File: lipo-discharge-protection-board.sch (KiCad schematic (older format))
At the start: 49 parts, among them J1 XT60, J2 Barrel_Jack, J3 2_PIN_SCREW, J4 Screw_Terminal_01x04, J5 Conn_02x02_Top_Bottom, Q1 AO3400A, Q2 AO3401A, Q3 AO3401A, Q4 AO3401A, Q5 AO3401A, U1 XL6009_module, U2 OPAMP

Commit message: Added alarm circuit
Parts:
- added D?: LED, symbol Device:LED
- added R?: 330R, Capacitor_SMD:C_0805_2012Metric_Pad1.18x1.45mm_HandSolder, symbol Device:R
- added R?: 220R, symbol Device:R
- added U?: L7805, symbol Regulator_Linear:L7805
- added U?: EL3H7, Package_DIP:DIP-4_W7.62mm, symbol Isolator:SFH617A-1
- Q2, Q3, Q4, Q5: LCSC C15127 -> AO3401A
- R1, R10, R11, R12, R13, R14, R15, R16, R2, R3, R4, R6, R7, R8, R9: footprint Resistor_SMD:R_0805_2012Metric_Pad1.20x1.40mm_HandSolder -> Capacitor_SMD:C_0805_2012Metric_Pad1.18x1.45mm_HandSolder
- R5: value 0R -> 0; footprint Resistor_SMD:R_0805_2012Metric_Pad1.20x1.40mm_HandSolder -> Capacitor_SMD:C_0805_2012Metric_Pad1.18x1.45mm_HandSolder
- U1: symbol lipo-discharge-protection-board-rescue:XL6009_module-xl6009_module -> xl6009_module:XL6009_module
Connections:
- net GND: now also R?.1, U?.2, U?.2 (GND)
- net at U?.3: now also U?.1 (IN)
- new net: D?.2 (A), R?.2, U?.3 (OUT)
- new net: R?.1, U?.1
- new net: D?.1 (K), R?.2
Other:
- moved on the sheet: J4, J5

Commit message: Added components for the alarm circuit and fixed wrong footprints
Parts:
- D2: renamed from D?; footprint (none) -> LED_SMD:LED_0805_2012Metric_Pad1.15x1.40mm_HandSolder
- R1, R10, R11, R12, R13, R14, R15, R16, R2, R3, R4, R5, R6, R7, R8, R9: footprint Capacitor_SMD:C_0805_2012Metric_Pad1.18x1.45mm_HandSolder -> Resistor_SMD:R_0805_2012Metric_Pad1.20x1.40mm_HandSolder
- R17, R18, R20: renamed from R?; footprint Capacitor_SMD:C_0805_2012Metric_Pad1.18x1.45mm_HandSolder -> Resistor_SMD:R_0805_2012Metric_Pad1.20x1.40mm_HandSolder
- R19: renamed from R?; footprint (none) -> Resistor_SMD:R_0805_2012Metric_Pad1.20x1.40mm_HandSolder
- U1: symbol xl6009_module:XL6009_module -> lipo-discharge-protection-board-rescue:XL6009_module-xl6009_module
- U4: renamed from U?; footprint (none) -> Package_TO_SOT_SMD:SOT-89-3_Handsoldering
- U5: renamed from U?; footprint Package_DIP:DIP-4_W7.62mm -> lipo-discharge-protection-board:SOIC127P700X210-4N
- gave numbers to parts that had none: 3

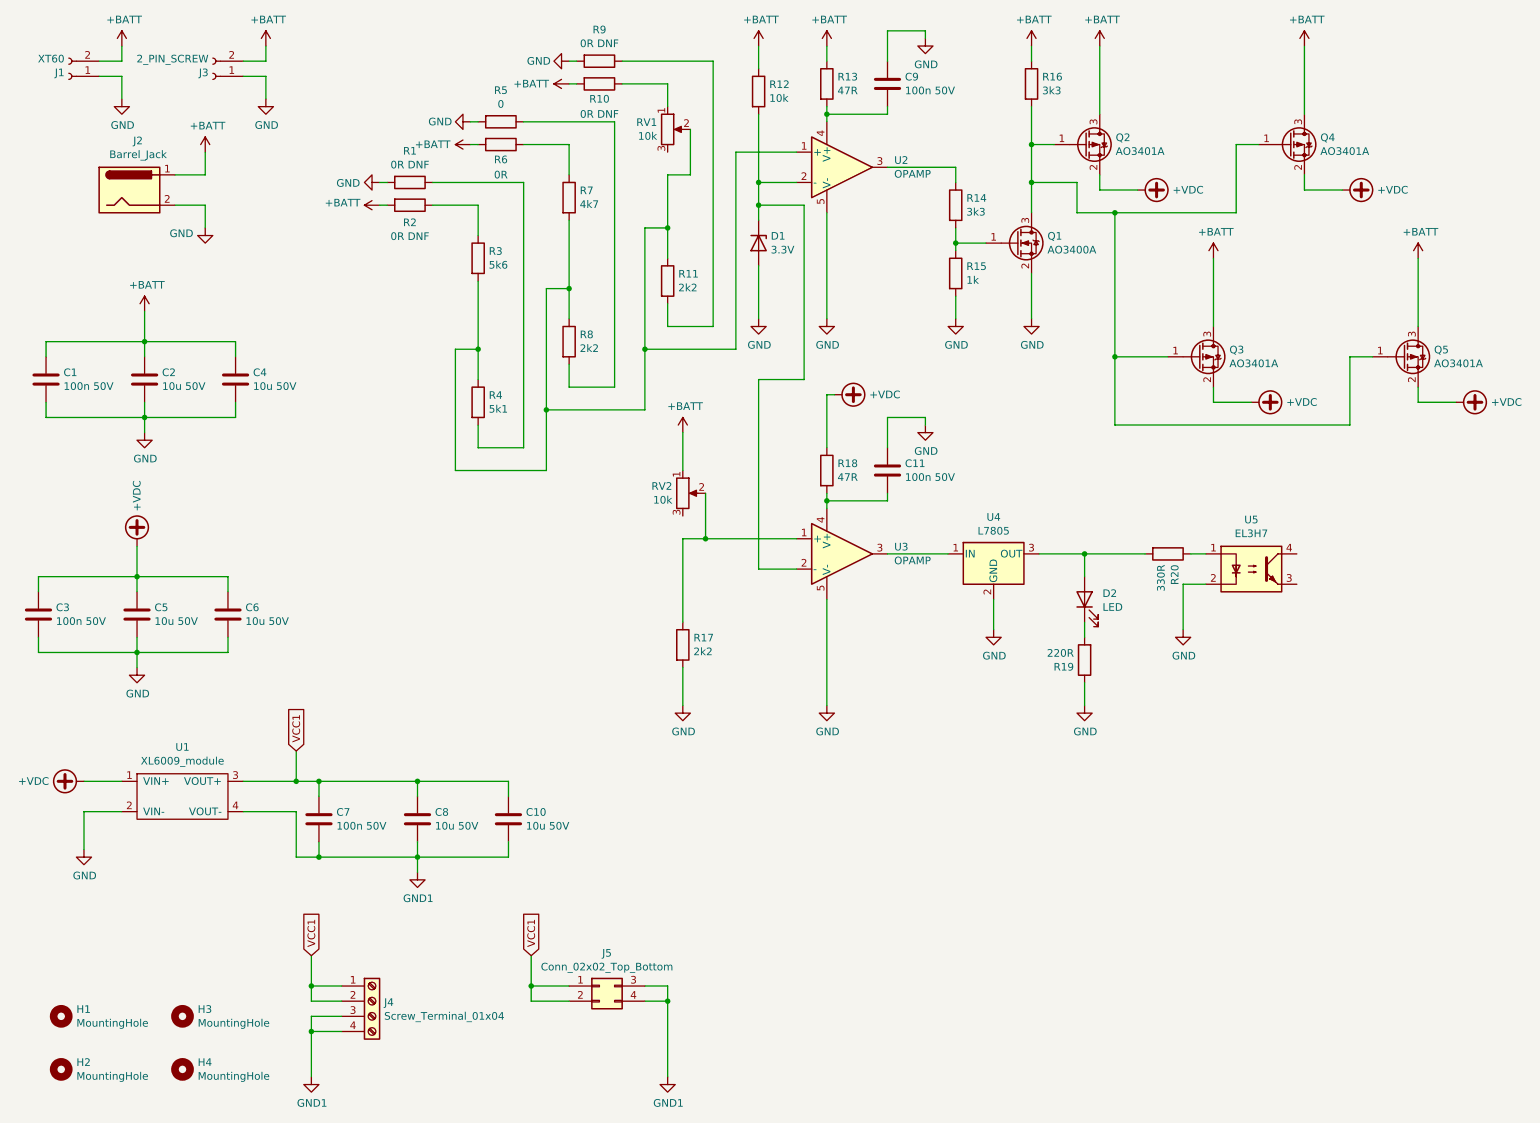
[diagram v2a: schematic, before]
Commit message: Added alarm circuit to PCB
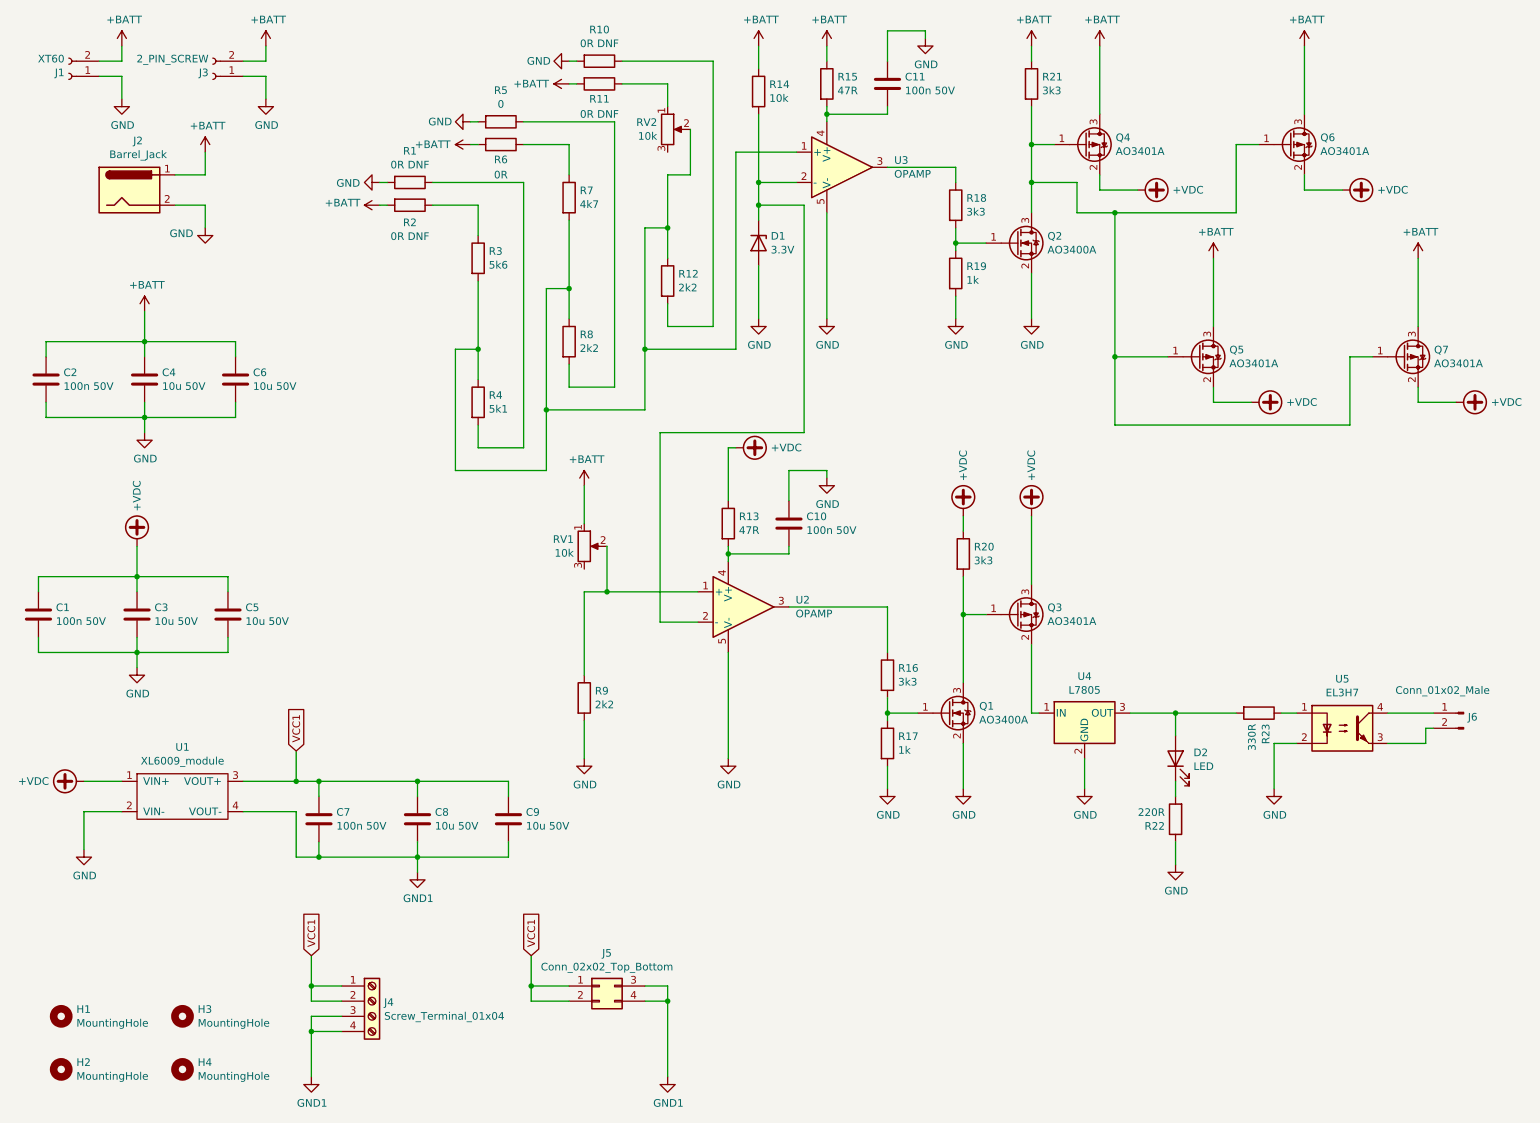
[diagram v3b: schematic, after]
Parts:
- added J6: Conn_01x02_Male, Connector_PinHeader_1.27mm:PinHeader_1x02_P1.27mm_Vertical, symbol Connector:Conn_01x02_Male
- added Q1: AO3400A, Package_TO_SOT_SMD:SOT-23, symbol Device:Q_NMOS_GSD
- added Q3: AO3401A, Package_TO_SOT_SMD:SOT-23, symbol Device:Q_PMOS_GSD
- added R16, R20: 3k3, Resistor_SMD:R_0805_2012Metric_Pad1.20x1.40mm_HandSolder, symbol Device:R
- added R17: 1k, Resistor_SMD:R_0805_2012Metric_Pad1.20x1.40mm_HandSolder, symbol Device:R
- renumbered C3 to C1, C11 to C10, C9 to C11, C1 to C2, C5 to C3, C2 to C4, C6 to C5, C4 to C6, C10 to C9, Q1 to Q2, Q2 to Q4, Q3 to Q5, Q4 to Q6, Q5 to Q7, R9 to R10, R10 to R11, R11 to R12, R18 to R13, R12 to R14, R13 to R15, R14 to R18, R15 to R19, R16 to R21, R19 to R22, R20 to R23, R17 to R9, RV2 to RV1, RV1 to RV2, U3 to U2, U2 to U3
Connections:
- net +VDC: now also Q3.3 (D), R20.1
- net GND: now also Q1.2 (S), R17.2
- net at U4.1 (IN): now also Q3.2 (S); no longer U2.3
- net at U5.3: now also J6.2 (Pin_2)
- net at U5.4: now also J6.1 (Pin_1)
- new net: Q1.1 (G), R16.2, R17.1
- new net: Q1.3 (D), Q3.1 (G), R20.2
- new net: R16.1, U2.3
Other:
- moved on the sheet: C10, D2, R13, R22, R23, R9, RV1, U2, U4, U5

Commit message: Added all project files and closing the project
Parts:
- removed U5: EL3H7, lipo-discharge-protection-board:SOIC127P700X210-4N, symbol Isolator:SFH617A-1
- added U5: 4N35, Package_DIP:DIP-6_W7.62mm, symbol Isolator:4N35
- D2: footprint LED_SMD:LED_0805_2012Metric_Pad1.15x1.40mm_HandSolder -> LED_THT:LED_D5.0mm; LCSC C2296 -> C84256
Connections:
- net GND: now also U5.2
- net at J6.1 (Pin_1): now also U5.5
- net at J6.2 (Pin_2): now also U5.4
- net at R23.1: now also U5.1
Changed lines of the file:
@@
 	7550 5650 7550 5850
-$Comp
-L Isolator:SFH617A-1 U5
-U 1 1 618EED7A
-P 9250 5450
-F 0 "U5" H 9250 5775 50  0000 C CNN
-F 1 "EL3H7" H 9250 5684 50  0000 C CNN
-F 2 "lipo-discharge-protection-board:SOIC127P700X210-4N" H 9050 5250 50  0001 L CIN
-F 3 "http://www.vishay.com/docs/83740/sfh617a.pdf" H 9250 5450 50  0001 L CNN
-F 4 "C32565" H 9250 5450 50  0001 C CNN "LCSC"
-	1    9250 5450
-	1    0    0    -1
-$EndComp
 $Comp
 L power:GND #PWR045
@@
 F 0 "D2" V 8189 5532 50  0000 R CNN
 F 1 "LED" V 8098 5532 50  0000 R CNN
-F 2 "LED_SMD:LED_0805_2012Metric_Pad1.15x1.40mm_HandSolder" H 8150 5650 50  0001 C CNN
+F 2 "LED_THT:LED_D5.0mm" H 8150 5650 50  0001 C CNN
 F 3 "~" H 8150 5650 50  0001 C CNN
-F 4 "C2296" V 8150 5650 50  0001 C CNN "LCSC"
+F 4 "C84256" V 8150 5650 50  0001 C CNN "LCSC"
 	1    8150 5650
 	0    -1   -1   0
@@
 	7200 4900 7200 5350
 Wire Wire Line
-	9550 5350 9850 5350
-Wire Wire Line
 	9850 5450 9800 5450
 Wire Wire Line
@@
 	1    0    0    -1
 $EndComp
+$Comp
+L Isolator:4N35 U5
+U 1 1 615D3201
+P 9250 5450
+F 0 "U5" H 9250 5775 50  0000 C CNN
+F 1 "4N35" H 9250 5684 50  0000 C CNN
+F 2 "Package_DIP:DIP-6_W7.62mm" H 9050 5250 50  0001 L CIN
+F 3 "https://www.vishay.com/docs/81181/4n35.pdf" H 9250 5450 50  0001 L CNN
+	1    9250 5450
+	1    0    0    -1
+$EndComp
+Wire Wire Line
+	9550 5450 9700 5450
+Wire Wire Line
+	9700 5450 9700 5350
+Wire Wire Line
+	9700 5350 9850 5350
 $EndSCHEMATC
